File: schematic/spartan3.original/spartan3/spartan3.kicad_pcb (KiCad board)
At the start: 2 copper layers, 215.9 x 160 mm, 240 parts, among them U1_clk_select_0 SPFT_Sliding_Switch-dynacore, U2 XC3S250E-4TQG144C

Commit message: PCB layout :: checked & updated
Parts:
- moved SW_reset_0 6.46 mm to (4.70, 102.3), turned to 90 degrees
- moved D_out_flags_C_out_0 2.50 mm to (144.7, 144.2)
- moved R_out_flags_C_out_0 2.50 mm to (144.7, 147.3)
- moved SW_read_register_0 0.92 mm to (44.1, 53.7)
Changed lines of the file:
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@@
   )
   (footprint "SR26 1-1-12P:SR26 1-1-12P" locked (layer "F.Cu")
-    (at 43.18 53.66)
+    (at 44.1 53.66)
     (property "Sheetfile" "spartan3.kicad_sch")
     (property "Sheetname" "")
@@
   )
   (footprint "Resistor_SMD:R_0805_2012Metric_Pad1.20x1.40mm_HandSolder" (layer "F.Cu")
-    (at 142.24 147.32)
+    (at 144.74 147.32)
     (descr "Resistor SMD 0805 (2012 Metric), square (rectangular) end terminal, IPC_7351 nominal with elongated pad for handsoldering. (Body size source: IPC-SM-782 page 72, https://www.pcb-3d.com/wordpress/wp-content/uploads/ipc-sm-782a_amendment_1_and_2.pdf), generated with kicad-footprint-generator")
     (tags "resistor handsolder")
@@
     )
   )
-  (footprint "Button_Switch_THT:SW_PUSH_6mm_H9.5mm" locked (layer "F.Cu")
-    (at 1.83 96.52)
+  (footprint "Button_Switch_THT:SW_PUSH_6mm_H9.5mm" (layer "F.Cu")
+    (at 4.6975 102.31 90)
     (descr "tactile push button, 6x6mm e.g. PHAP33xx series, height=9.5mm")
     (tags "tact sw push 6mm")
@@
     (property "Sheetname" "")
     (attr through_hole)
-    (fp_text reference "SW_reset_0" (at 3.25 -2.83) (layer "F.SilkS")
+    (fp_text reference "SW_reset_0" (at 3.25 -2.83 90) (layer "F.SilkS")
       (effects (font (size 1 1) (thickness 0.15)))
     )
-    (fp_text value "SW_Push" (at 3.75 6.7) (layer "F.Fab")
+    (fp_text value "SW_Push" (at 3.75 6.7 90) (layer "F.Fab")
       (effects (font (size 1 1) (thickness 0.15)))
     )
-    (fp_text user "${REFERENCE}" (at 3.25 2.25) (layer "F.Fab")
+    (fp_text user "${REFERENCE}" (at 3.25 2.25 90) (layer "F.Fab")
       (effects (font (size 1 1) (thickness 0.15)))
     )
@@
     (fp_line (start 6.25 5.25) (end 0.25 5.25) (layer "F.Fab") (width 0.1))
     (fp_circle (center 3.25 2.25) (end 1.25 2.5) (layer "F.Fab") (width 0.1) (fill none))
-    (pad "1" thru_hole circle locked (at 6.5 0 90) (size 2 2) (drill 1.1) (layers *.Cu *.Mask)
+    (pad "1" thru_hole circle locked (at 6.5 0 180) (size 2 2) (drill 1.1) (layers *.Cu *.Mask)
       (net 152 "reset") (pinfunction "1") (pintype "passive"))
-    (pad "1" thru_hole circle locked (at 0 0 90) (size 2 2) (drill 1.1) (layers *.Cu *.Mask)
+    (pad "1" thru_hole circle locked (at 0 0 180) (size 2 2) (drill 1.1) (layers *.Cu *.Mask)
       (net 152 "reset") (pinfunction "1") (pintype "passive"))
-    (pad "2" thru_hole circle locked (at 0 4.5 90) (size 2 2) (drill 1.1) (layers *.Cu *.Mask)
+    (pad "2" thru_hole circle locked (at 0 4.5 180) (size 2 2) (drill 1.1) (layers *.Cu *.Mask)
       (net 2 "GND") (pinfunction "2") (pintype "passive"))
-    (pad "2" thru_hole circle locked (at 6.5 4.5 90) (size 2 2) (drill 1.1) (layers *.Cu *.Mask)
+    (pad "2" thru_hole circle locked (at 6.5 4.5 180) (size 2 2) (drill 1.1) (layers *.Cu *.Mask)
       (net 2 "GND") (pinfunction "2") (pintype "passive"))
     (model "${KICAD6_3DMODEL_DIR}/Button_Switch_THT.3dshapes/SW_PUSH_6mm_H9.5mm.wrl"
@@
   )
   (footprint "LED_SMD:LED_0805_2012Metric_Pad1.15x1.40mm_HandSolder" locked (layer "F.Cu")
-    (at 142.24 144.24)
+    (at 144.74 144.24)
     (descr "LED SMD 0805 (2012 Metric), square (rectangular) end terminal, IPC_7351 nominal, (Body size source: https://docs.google.com/spreadsheets/d/1BsfQQcO9C6DZCsRaXUlFlo91Tg2WpOkGARC1WS5S8t0/edit?usp=sharing), generated with kicad-footprint-generator")
     (tags "LED handsolder")

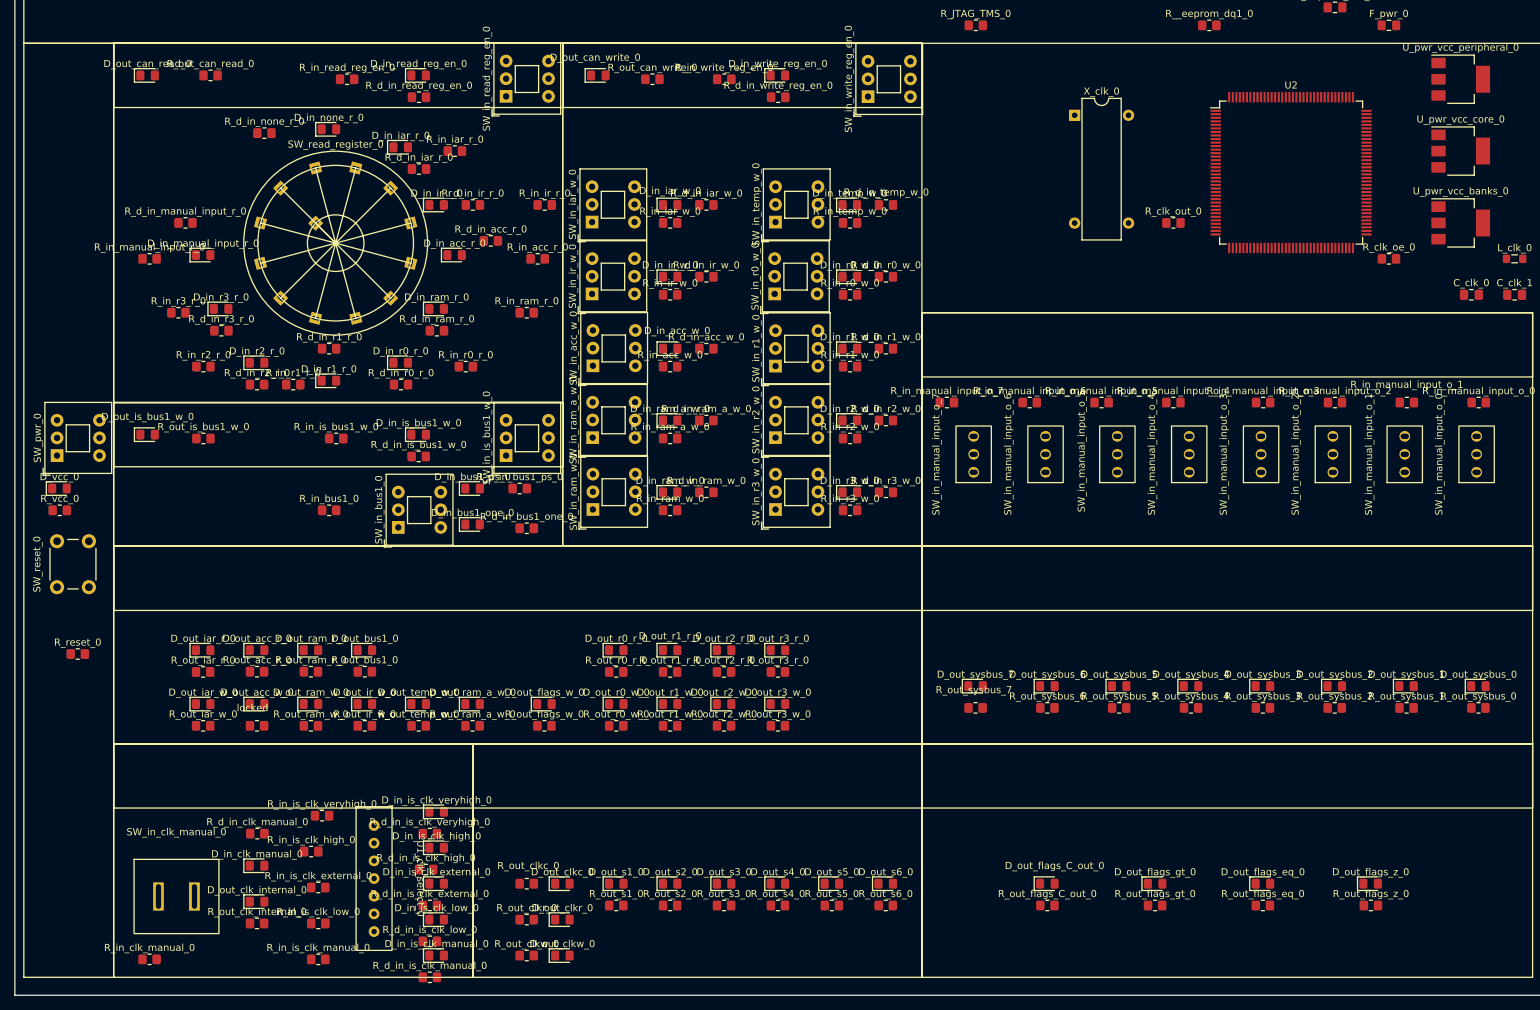
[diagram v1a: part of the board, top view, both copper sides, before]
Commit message: Schematic :: LED R/SW_DPDT updated. PCB layout :: logic, non FPGA connections implemented
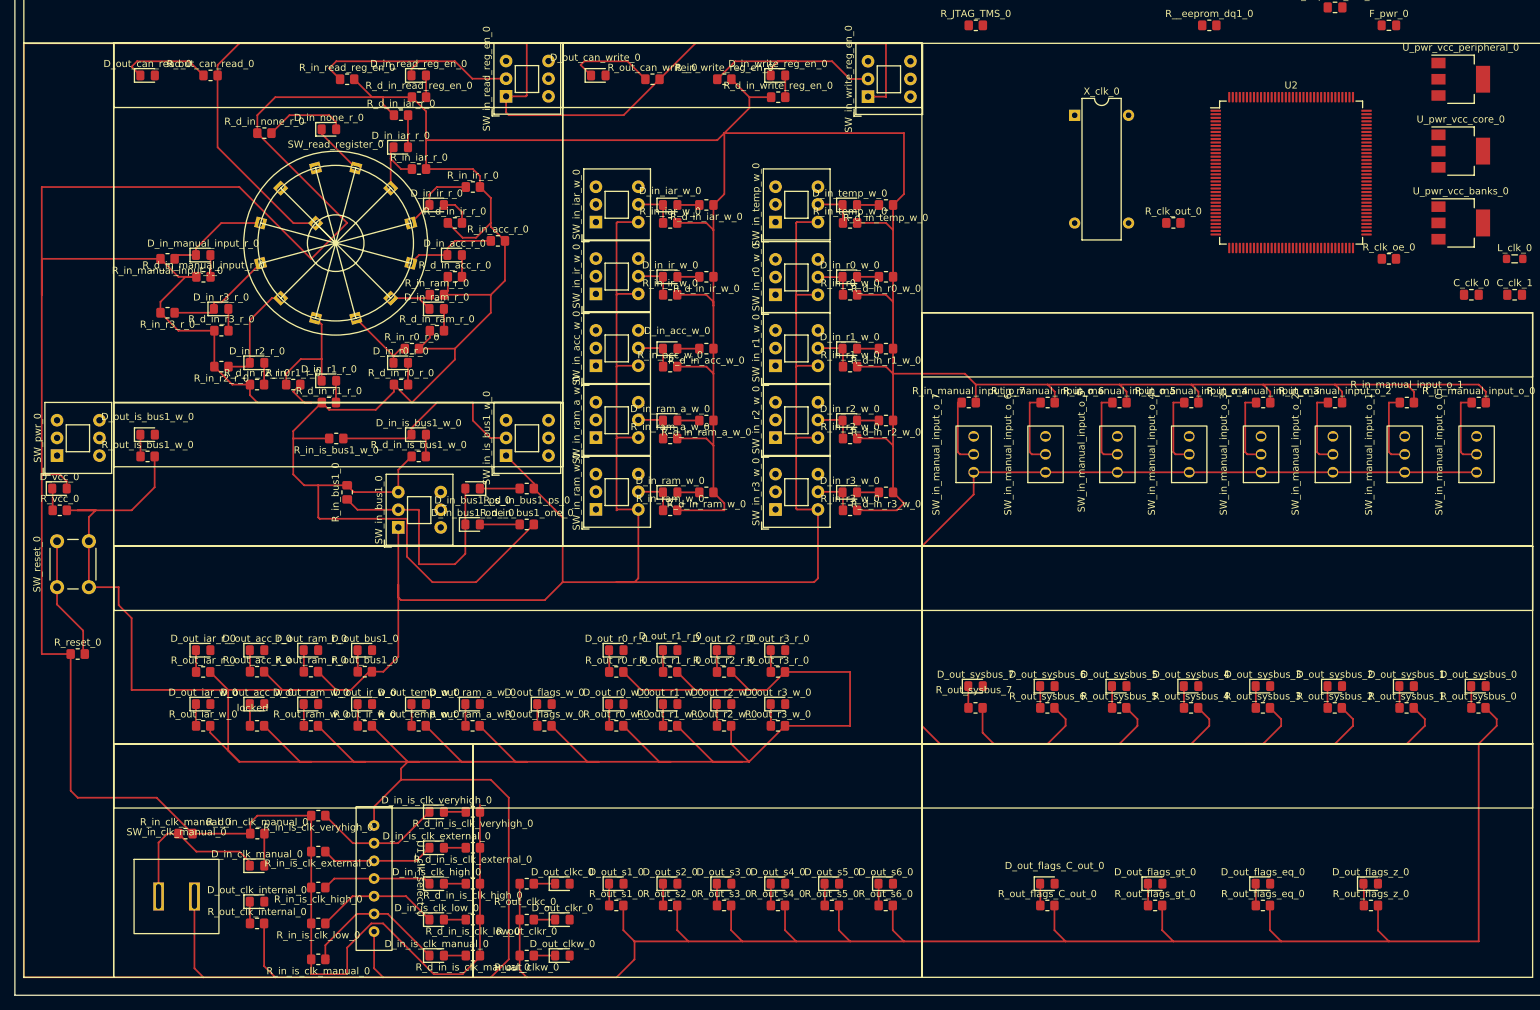
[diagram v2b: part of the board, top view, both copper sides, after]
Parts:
- R_d_in_acc_r_0, R_d_in_acc_w_0, R_d_in_bus1_one_0, R_d_in_bus1_ps_0, R_d_in_clk_manual_0, R_d_in_iar_r_0, R_d_in_iar_w_0, R_d_in_ir_r_0, R_d_in_ir_w_0, R_d_in_is_bus1_w_0, R_d_in_is_clk_external_0, R_d_in_is_clk_high_0, R_d_in_is_clk_low_0, R_d_in_is_clk_manual_0, R_d_in_is_clk_veryhigh_0, R_d_in_manual_input_r_0, R_d_in_none_r_0, R_d_in_r0_r_0, R_d_in_r0_w_0, R_d_in_r1_r_0, R_d_in_r1_w_0, R_d_in_r2_r_0, R_d_in_r2_w_0, R_d_in_r3_r_0, R_d_in_r3_w_0, R_d_in_ram_a_w_0, R_d_in_ram_r_0, R_d_in_ram_w_0, R_d_in_read_reg_en_0, R_d_in_temp_w_0, R_d_in_write_reg_en_0, R_out_acc_r_0, R_out_bus1_0, R_out_can_read_0, R_out_can_write_0, R_out_clk_internal_0, R_out_clkc_0, R_out_clkr_0, R_out_clkw_0, R_out_flags_C_out_0, R_out_flags_eq_0, R_out_flags_gt_0, R_out_flags_w_0, R_out_flags_z_0, R_out_iar_r_0, R_out_iar_w_0, R_out_ir_w_0, R_out_is_bus1_w_0, R_out_r0_r_0, R_out_r0_w_0, R_out_r1_r_0, R_out_r1_w_0, R_out_r2_r_0, R_out_r2_w_0, R_out_r3_r_0, R_out_r3_w_0, R_out_ram_a_w_0, R_out_ram_r_0, R_out_ram_w_0, R_out_s1_0, R_out_s2_0, R_out_s3_0, R_out_s4_0, R_out_s5_0, R_out_s6_0, R_out_sysbus_0, R_out_sysbus_1, R_out_sysbus_2, R_out_sysbus_3, R_out_sysbus_4, R_out_sysbus_5, R_out_sysbus_6, R_out_sysbus_7, R_out_temp_w_0, R_vcc_0, locked: value 100R -> 68R
- moved R_in_clk_manual_0 18.5 mm to (22.9, 137.2)
- moved R_in_ram_r_0 13.0 mm to (58.4, 61.0)
- moved R_in_ir_r_0 10.5 mm to (63.5, 45.7)
- moved R_d_in_is_clk_external_0 10.2 mm to (63.5, 139.2), turned to 180 degrees
- moved R_out_is_bus1_w_0 8.30 mm to (17.5, 83.8)
- moved R_d_in_manual_input_r_0 8.03 mm to (25.4, 58.4)
- moved R_in_r0_r_0 8.03 mm to (54.9, 68.6)
- moved R_d_in_iar_r_0 8.03 mm to (53.3, 35.6)
- moved R_d_in_r1_r_0 7.62 mm to (43.1, 76.2)
- moved R_d_in_acc_r_0 7.18 mm to (61.0, 58.4)
- moved R_d_in_is_clk_high_0 6.92 mm to (63.5, 144.2), turned to 180 degrees
- moved R_d_in_is_clk_low_0 6.82 mm to (63.5, 149.3), turned to 180 degrees
- moved R_d_in_is_clk_manual_0 6.82 mm to (63.5, 154.4), turned to 180 degrees
- moved R_d_in_is_clk_veryhigh_0 6.82 mm to (63.5, 134.1), turned to 180 degrees
- moved R_in_acc_r_0 6.17 mm to (67.0, 53.3)
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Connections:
- SW_in_acc_w_0 pad 1: GND -> (no net)
- SW_in_acc_w_0 pad 2: in_acc_w -> (no net)
- SW_in_acc_w_0 pad 3: unconnected-(SW_in_acc_w_0-Pad3) -> (no net)
- SW_in_acc_w_0 pad 4: (no net) -> GND
- SW_in_acc_w_0 pad 5: (no net) -> in_acc_w
- SW_in_acc_w_0 pad 6: (no net) -> unconnected-(SW_in_acc_w_0-Pad6)
- SW_in_iar_w_0 pad 1: GND -> (no net)
- SW_in_iar_w_0 pad 2: in_iar_w -> (no net)
- SW_in_iar_w_0 pad 3: unconnected-(SW_in_iar_w_0-Pad3) -> (no net)
- SW_in_iar_w_0 pad 4: (no net) -> GND
- SW_in_iar_w_0 pad 5: (no net) -> in_iar_w
- SW_in_iar_w_0 pad 6: (no net) -> unconnected-(SW_in_iar_w_0-Pad6)
- SW_in_ir_w_0 pad 1: GND -> (no net)
- SW_in_ir_w_0 pad 2: in_ir_w -> (no net)
- SW_in_ir_w_0 pad 3: unconnected-(SW_in_ir_w_0-Pad3) -> (no net)
- SW_in_ir_w_0 pad 4: (no net) -> GND
- SW_in_ir_w_0 pad 5: (no net) -> in_ir_w
- SW_in_ir_w_0 pad 6: (no net) -> unconnected-(SW_in_ir_w_0-Pad6)
- SW_in_r0_w_0 pad 1: GND -> (no net)
- SW_in_r0_w_0 pad 2: in_r0_w -> (no net)
- SW_in_r0_w_0 pad 3: unconnected-(SW_in_r0_w_0-Pad3) -> (no net)
- SW_in_r0_w_0 pad 4: (no net) -> GND
- SW_in_r0_w_0 pad 5: (no net) -> in_r0_w
- SW_in_r0_w_0 pad 6: (no net) -> unconnected-(SW_in_r0_w_0-Pad6)
- SW_in_r1_w_0 pad 1: GND -> (no net)
- SW_in_r1_w_0 pad 2: in_r1_w -> (no net)
- SW_in_r1_w_0 pad 3: unconnected-(SW_in_r1_w_0-Pad3) -> (no net)
- SW_in_r1_w_0 pad 4: (no net) -> GND
- SW_in_r1_w_0 pad 5: (no net) -> in_r1_w
- SW_in_r1_w_0 pad 6: (no net) -> unconnected-(SW_in_r1_w_0-Pad6)
- SW_in_r2_w_0 pad 1: GND -> (no net)
- SW_in_r2_w_0 pad 2: in_r2_w -> (no net)
- SW_in_r2_w_0 pad 3: unconnected-(SW_in_r2_w_0-Pad3) -> (no net)
- SW_in_r2_w_0 pad 4: (no net) -> GND
- SW_in_r2_w_0 pad 5: (no net) -> in_r2_w
- SW_in_r2_w_0 pad 6: (no net) -> unconnected-(SW_in_r2_w_0-Pad6)
- SW_in_r3_w_0 pad 1: GND -> (no net)
- SW_in_r3_w_0 pad 2: in_r3_w -> (no net)
- SW_in_r3_w_0 pad 3: unconnected-(SW_in_r3_w_0-Pad3) -> (no net)
- SW_in_r3_w_0 pad 4: (no net) -> GND
- SW_in_r3_w_0 pad 5: (no net) -> in_r3_w
- SW_in_r3_w_0 pad 6: (no net) -> unconnected-(SW_in_r3_w_0-Pad6)
- SW_in_ram_a_w_0 pad 1: GND -> (no net)
- SW_in_ram_a_w_0 pad 2: in_ram_a_w -> (no net)
- SW_in_ram_a_w_0 pad 3: unconnected-(SW_in_ram_a_w_0-Pad3) -> (no net)
- SW_in_ram_a_w_0 pad 4: (no net) -> GND
- SW_in_ram_a_w_0 pad 5: (no net) -> in_ram_a_w
- SW_in_ram_a_w_0 pad 6: (no net) -> unconnected-(SW_in_ram_a_w_0-Pad6)
- SW_in_ram_w_0 pad 1: GND -> (no net)
- SW_in_ram_w_0 pad 2: in_ram_w -> (no net)
- SW_in_ram_w_0 pad 3: unconnected-(SW_in_ram_w_0-Pad3) -> (no net)
- SW_in_ram_w_0 pad 4: (no net) -> GND
- SW_in_ram_w_0 pad 5: (no net) -> in_ram_w
- SW_in_ram_w_0 pad 6: (no net) -> unconnected-(SW_in_ram_w_0-Pad6)
- SW_in_temp_w_0 pad 1: GND -> (no net)
- SW_in_temp_w_0 pad 2: in_temp_w -> (no net)
- SW_in_temp_w_0 pad 3: unconnected-(SW_in_temp_w_0-Pad3) -> (no net)
- SW_in_temp_w_0 pad 4: (no net) -> GND
- SW_in_temp_w_0 pad 5: (no net) -> in_temp_w
- SW_in_temp_w_0 pad 6: (no net) -> unconnected-(SW_in_temp_w_0-Pad6)
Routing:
- net GND: track 0.00 -> 1549.1 mm
- net VCC: track 0.00 -> 921.7 mm
- net in_bus1: track 0.00 -> 34.8 mm
- net in_read_reg_en: track 0.00 -> 33.6 mm
- net in_is_bus1_w: track 0.00 -> 29.2 mm
- net in_write_reg_en: track 0.00 -> 28.4 mm
- net in_clk_manual: track 0.00 -> 23.2 mm
- net in_is_clk_manual: track 0.00 -> 21.4 mm
- net in_is_clk_veryhigh: track 0.00 -> 18.2 mm
- net in_is_clk_low: track 0.00 -> 17.7 mm
- net reset: track 0.00 -> 17.6 mm
- net in_r1_r: track 0.00 -> 16.6 mm
- net in_is_clk_external: track 0.00 -> 16.0 mm
- net in_r3_r: track 0.00 -> 15.6 mm
- net in_is_clk_high: track 0.00 -> 15.5 mm
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
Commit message: Schematics :: J_CONTROL added. PCB layout :: updated
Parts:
- added J_CONTROL_0: Conn_01x25_Male, Connector_PinHeader_2.54mm:PinHeader_1x25_P2.54mm_Vertical, F.Cu at (210.8, 5.08)
- U2: moved to B.Cu
- moved X_clk_0 162.0 mm to (14.0, 125.7), turned to 90 degrees
- moved R_clk_out_0 82.9 mm to (109.2, -12.7)
- moved J_pwr_0 59.6 mm to (154.1, -19.4)
- moved U_pwr_vcc_core_0 58.8 mm to (196.6, -17.8)
- moved U_pwr_vcc_peripheral_0 58.8 mm to (196.6, -27.9)
- moved U_pwr_vcc_banks_0 58.8 mm to (196.6, -7.62)
- moved C_clk_0 56.1 mm to (260.6, 55.9)
- moved R_clk_oe_0 56.1 mm to (248.9, 50.8)
- moved C_eeprom_vcc_0 51.6 mm to (147.4, -14.6)
- moved F_pwr_0 51.6 mm to (155.0, -12.1)
- moved R_JTAG_TCK_0 51.6 mm to (99.2, -17.2)
- moved R_JTAG_TDI_0 51.6 mm to (81.4, -24.8)
- moved R_JTAG_TDO_0 51.6 mm to (114.4, -17.2)
- moved R_JTAG_TMS_0 51.6 mm to (96.6, -12.1)
- moved R__eeprom_dq1_0 51.6 mm to (129.6, -12.1)
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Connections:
- net Net-(R_JTAG_TCK_0-Pad2) renamed P110
- net Net-(R_JTAG_TDI_0-Pad2) renamed P144
- net Net-(R_JTAG_TDO_0-Pad2) renamed P109
- net Net-(R_JTAG_TMS_0-Pad2) renamed P108
- net Net-(U2-Pad115) renamed VCC_core
- net clk renamed P56
- net eeprom_spi_clk renamed P71
- net eeprom_spi_dout renamed P63
- U2 pad 1: unconnected-(U2-Pad1) -> P1
- U2 pad 10: unconnected-(U2-Pad10) -> P10
- U2 pad 101: unconnected-(U2-Pad101) -> P101
- U2 pad 103: unconnected-(U2-Pad103) -> P103
- U2 pad 104: unconnected-(U2-Pad104) -> P104
- U2 pad 105: unconnected-(U2-Pad105) -> P105
- U2 pad 106: unconnected-(U2-Pad106) -> P106
- U2 pad 107: unconnected-(U2-Pad107) -> P107
- U2 pad 111: unconnected-(U2-Pad111) -> P111
- U2 pad 112: unconnected-(U2-Pad112) -> P112
- U2 pad 113: unconnected-(U2-Pad113) -> P113
- U2 pad 114: unconnected-(U2-Pad114) -> P114
- U2 pad 116: unconnected-(U2-Pad116) -> P116
- U2 pad 117: unconnected-(U2-Pad117) -> P117
- U2 pad 119: unconnected-(U2-Pad119) -> P119
- U2 pad 12: unconnected-(U2-Pad12) -> P12
- U2 pad 120: unconnected-(U2-Pad120) -> P120
- U2 pad 122: unconnected-(U2-Pad122) -> P122
- U2 pad 123: unconnected-(U2-Pad123) -> P123
- U2 pad 124: unconnected-(U2-Pad124) -> P124
- U2 pad 125: unconnected-(U2-Pad125) -> P125
- U2 pad 126: unconnected-(U2-Pad126) -> P126
- U2 pad 128: unconnected-(U2-Pad128) -> P128
- U2 pad 129: unconnected-(U2-Pad129) -> P129
- U2 pad 130: unconnected-(U2-Pad130) -> P130
- U2 pad 131: unconnected-(U2-Pad131) -> P131
- U2 pad 132: unconnected-(U2-Pad132) -> P132
- U2 pad 134: unconnected-(U2-Pad134) -> P134
- U2 pad 135: unconnected-(U2-Pad135) -> P135
- U2 pad 136: unconnected-(U2-Pad136) -> P136
- U2 pad 139: unconnected-(U2-Pad139) -> P139
- U2 pad 14: unconnected-(U2-Pad14) -> P14
- U2 pad 140: unconnected-(U2-Pad140) -> P140
- U2 pad 141: unconnected-(U2-Pad141) -> P141
- U2 pad 142: unconnected-(U2-Pad142) -> P142
- U2 pad 143: unconnected-(U2-Pad143) -> P143
- U2 pad 15: unconnected-(U2-Pad15) -> P15
- U2 pad 16: unconnected-(U2-Pad16) -> P16
- U2 pad 17: unconnected-(U2-Pad17) -> P17
- U2 pad 18: unconnected-(U2-Pad18) -> P18
- U2 pad 2: unconnected-(U2-Pad2) -> P2
- U2 pad 20: unconnected-(U2-Pad20) -> P20
- U2 pad 21: unconnected-(U2-Pad21) -> P21
- U2 pad 22: unconnected-(U2-Pad22) -> P22
- U2 pad 23: unconnected-(U2-Pad23) -> P23
- U2 pad 24: unconnected-(U2-Pad24) -> P24
- U2 pad 25: unconnected-(U2-Pad25) -> P25
- U2 pad 26: unconnected-(U2-Pad26) -> P26
- U2 pad 29: unconnected-(U2-Pad29) -> P29
- U2 pad 3: unconnected-(U2-Pad3) -> P3
- U2 pad 31: unconnected-(U2-Pad31) -> P31
- U2 pad 32: unconnected-(U2-Pad32) -> P32
- U2 pad 33: unconnected-(U2-Pad33) -> P33
- U2 pad 34: unconnected-(U2-Pad34) -> P34
- U2 pad 35: unconnected-(U2-Pad35) -> P35
- U2 pad 36: unconnected-(U2-Pad36) -> P36
- U2 pad 38: unconnected-(U2-Pad38) -> P38
- U2 pad 39: eprom_spi_cs_n -> P39
- U2 pad 4: unconnected-(U2-Pad4) -> P4
- U2 pad 40: unconnected-(U2-Pad40) -> P40
- U2 pad 41: unconnected-(U2-Pad41) -> P41
- U2 pad 43: unconnected-(U2-Pad43) -> P43
- U2 pad 44: eprom_spi_din -> P44
- U2 pad 47: unconnected-(U2-Pad47) -> P47
- U2 pad 48: unconnected-(U2-Pad48) -> P48
- U2 pad 5: unconnected-(U2-Pad5) -> P5
- U2 pad 50: unconnected-(U2-Pad50) -> P50
- U2 pad 51: unconnected-(U2-Pad51) -> P51
- U2 pad 52: unconnected-(U2-Pad52) -> P52
- U2 pad 53: unconnected-(U2-Pad53) -> P53
- U2 pad 54: unconnected-(U2-Pad54) -> P54
- U2 pad 57: unconnected-(U2-Pad57) -> P57
- U2 pad 58: unconnected-(U2-Pad58) -> P58
- U2 pad 59: unconnected-(U2-Pad59) -> P59
- U2 pad 6: unconnected-(U2-Pad6) -> P6
- U2 pad 60: unconnected-(U2-Pad60) -> P60
- U2 pad 62: unconnected-(U2-Pad62) -> P62
- U2 pad 66: unconnected-(U2-Pad66) -> P66
- U2 pad 67: unconnected-(U2-Pad67) -> P67
- U2 pad 68: unconnected-(U2-Pad68) -> P68
- U2 pad 69: unconnected-(U2-Pad69) -> P69
- U2 pad 7: unconnected-(U2-Pad7) -> P7
- U2 pad 70: unconnected-(U2-Pad70) -> P70
- U2 pad 72: unconnected-(U2-Pad72) -> P72
- U2 pad 74: unconnected-(U2-Pad74) -> P74
- U2 pad 75: unconnected-(U2-Pad75) -> P75
- U2 pad 76: unconnected-(U2-Pad76) -> P76
- U2 pad 77: unconnected-(U2-Pad77) -> P77
- U2 pad 78: unconnected-(U2-Pad78) -> P78
- U2 pad 8: unconnected-(U2-Pad8) -> P8
- U2 pad 81: unconnected-(U2-Pad81) -> P81
- U2 pad 82: unconnected-(U2-Pad82) -> P82
- U2 pad 83: unconnected-(U2-Pad83) -> P83
- U2 pad 84: unconnected-(U2-Pad84) -> P84
- U2 pad 85: unconnected-(U2-Pad85) -> P85
- U2 pad 86: unconnected-(U2-Pad86) -> P86
- U2 pad 87: unconnected-(U2-Pad87) -> P87
- U2 pad 88: unconnected-(U2-Pad88) -> P88
- U2 pad 89: unconnected-(U2-Pad89) -> P89
- U2 pad 91: unconnected-(U2-Pad91) -> P91
- U2 pad 92: unconnected-(U2-Pad92) -> P92
- U2 pad 93: unconnected-(U2-Pad93) -> P93
- U2 pad 94: unconnected-(U2-Pad94) -> P94
- U2 pad 95: unconnected-(U2-Pad95) -> P95
- U2 pad 96: unconnected-(U2-Pad96) -> P96
- U2 pad 97: unconnected-(U2-Pad97) -> P97
- U2 pad 98: unconnected-(U2-Pad98) -> P98
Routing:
- net P96: track 0.00 -> 0.80 mm
- net P117: track 0.00 -> 0.80 mm
- net P110: track 0.00 -> 0.80 mm
- net VCC_core: track 0.00 -> 0.62 mm
